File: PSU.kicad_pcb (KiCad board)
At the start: 2 copper layers, 170 x 60 mm, 55 parts, among them J1 ~12VAC_A, J10 GND, J11 -12V, J12 +5V, J2 ~12VAC_A, J3 ~12VAC_B, J4 ~12VAC_B, J9 +12V, U1 LM317_TO-220, U2 LM317_TO-220, U3 LM337_TO220

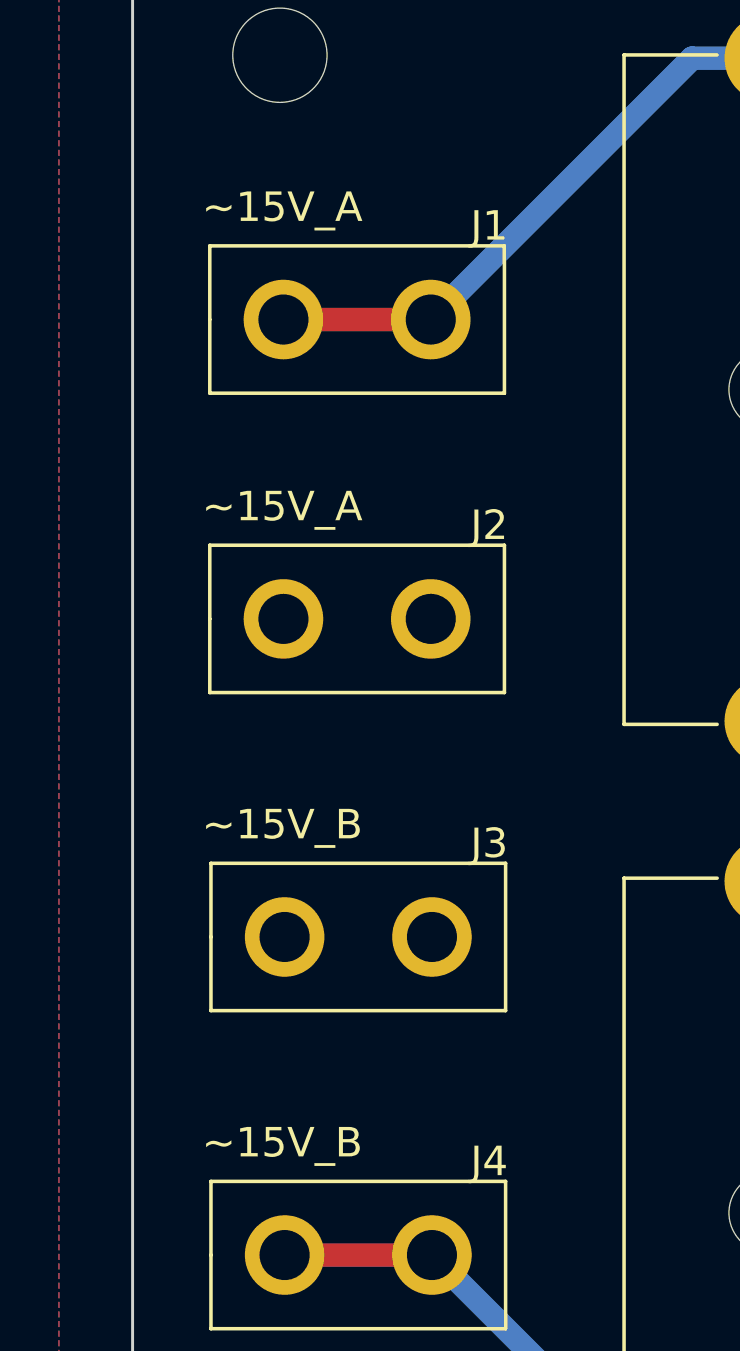
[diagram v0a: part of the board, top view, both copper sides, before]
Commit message: Swap rectifier diodes for larger ones. Change input terminal text to be more legible.
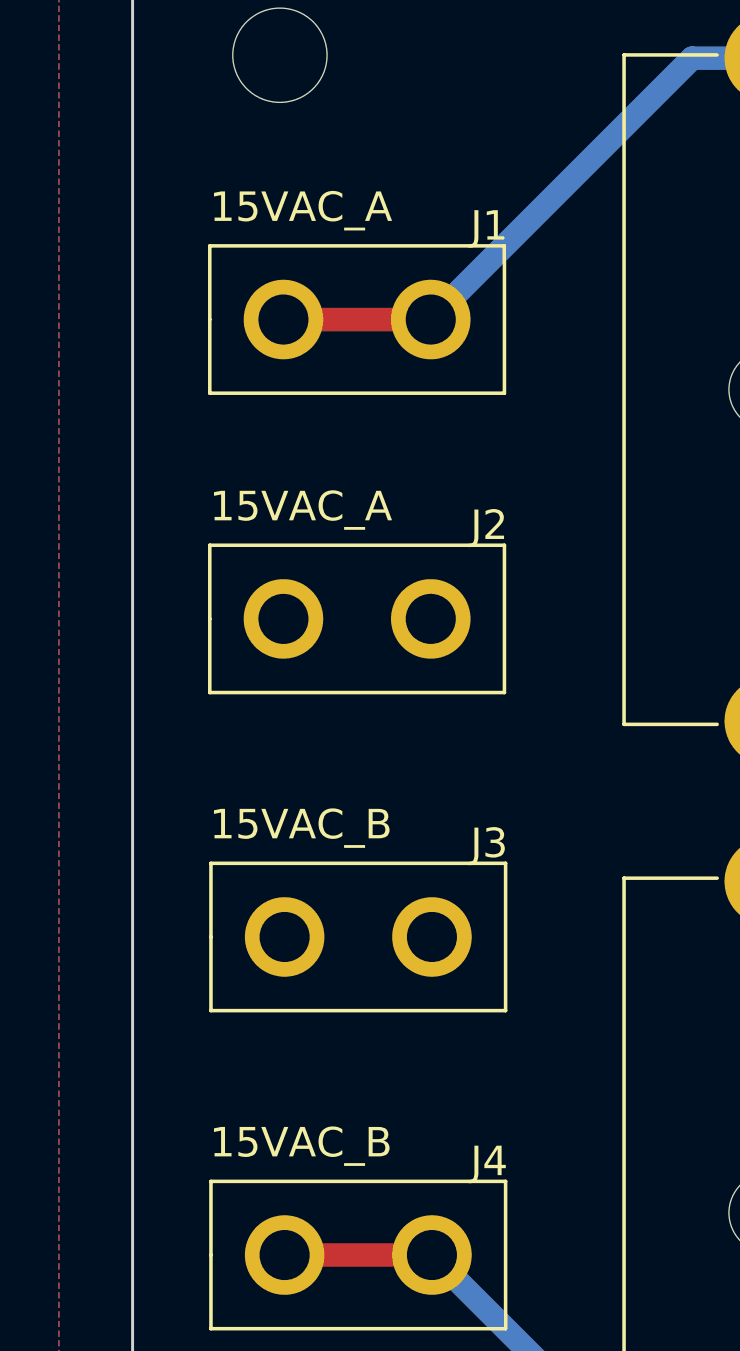
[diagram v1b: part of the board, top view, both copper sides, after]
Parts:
- D1, D2, D3, D4: value 1N4004 -> 1N5060
- F1, F2: value 6.3A fast -> fast
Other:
- board text added: "15VAC_A"
- board text added: "15VAC_B"
- board text removed: "~15V_A"
- board text removed: "~15V_B"
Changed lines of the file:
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@@
       (effects (font (size 1 1) (thickness 0.15)))
     )
-    (fp_text value "1N4004" (at 5.08 0.762) (layer "F.Fab")
+    (fp_text value "1N5060" (at 5.08 0.762) (layer "F.Fab")
       (effects (font (size 1 1) (thickness 0.15)))
     )
@@
       (effects (font (size 1 1) (thickness 0.15)))
     )
-    (fp_text value "1N4004" (at 5.08 0.762) (layer "F.Fab")
+    (fp_text value "1N5060" (at 5.08 0.762) (layer "F.Fab")
       (effects (font (size 1 1) (thickness 0.15)))
     )
@@
       (effects (font (size 1 1) (thickness 0.15)))
     )
-    (fp_text value "1N4004" (at 5.08 0.762) (layer "F.Fab")
+    (fp_text value "1N5060" (at 5.08 0.762) (layer "F.Fab")
       (effects (font (size 1 1) (thickness 0.15)))
     )
@@
       (effects (font (size 1 1) (thickness 0.15)))
     )
-    (fp_text value "6.3A fast" (at 11.25 3.81 90) (layer "F.Fab")
+    (fp_text value "fast" (at 11.25 3.81 90) (layer "F.Fab")
       (effects (font (size 1 1) (thickness 0.15)))
     )
@@
       (effects (font (size 1 1) (thickness 0.15)))
     )
-    (fp_text value "1N4004" (at 5.08 0.762) (layer "F.Fab")
+    (fp_text value "1N5060" (at 5.08 0.762) (layer "F.Fab")
       (effects (font (size 1 1) (thickness 0.15)))
     )
@@
       (effects (font (size 1 1) (thickness 0.15)))
     )
-    (fp_text value "6.3A fast" (at 12.012 -3.81 90) (layer "F.Fab")
+    (fp_text value " fast" (at 12.012 -3.81 90) (layer "F.Fab")
       (effects (font (size 1 1) (thickness 0.15)))
     )
@@
   (gr_line (start 0 0) (end 0 60) (layer "Edge.Cuts") (width 0.1))
   (gr_line (start 0 0) (end 170 0) (layer "Edge.Cuts") (width 0.1))
-  (gr_text "~15V_A" (at 5.08 10.16) (layer "F.SilkS")
+  (gr_text "15VAC_A" (at 5.715 10.16) (layer "F.SilkS")
     (effects (font (size 1 1) (thickness 0.15)))
   )
@@
     (effects (font (size 1 1) (thickness 0.15)))
   )
-  (gr_text "~15V_B" (at 5.08 31.115) (layer "F.SilkS")
+  (gr_text "15VAC_B" (at 5.715 31.115) (layer "F.SilkS")
     (effects (font (size 1 1) (thickness 0.15)))
   )
@@
     (effects (font (size 1 1) (thickness 0.15)))
   )
-  (gr_text "~15V_A" (at 5.08 20.32) (layer "F.SilkS")
+  (gr_text "15VAC_A" (at 5.715 20.32) (layer "F.SilkS")
     (effects (font (size 1 1) (thickness 0.15)))
   )
@@
     (effects (font (size 1 1) (thickness 0.15)))
   )
-  (gr_text "~15V_B" (at 5.08 41.91) (layer "F.SilkS")
+  (gr_text "15VAC_B" (at 5.715 41.91) (layer "F.SilkS")
     (effects (font (size 1 1) (thickness 0.15)))
   )

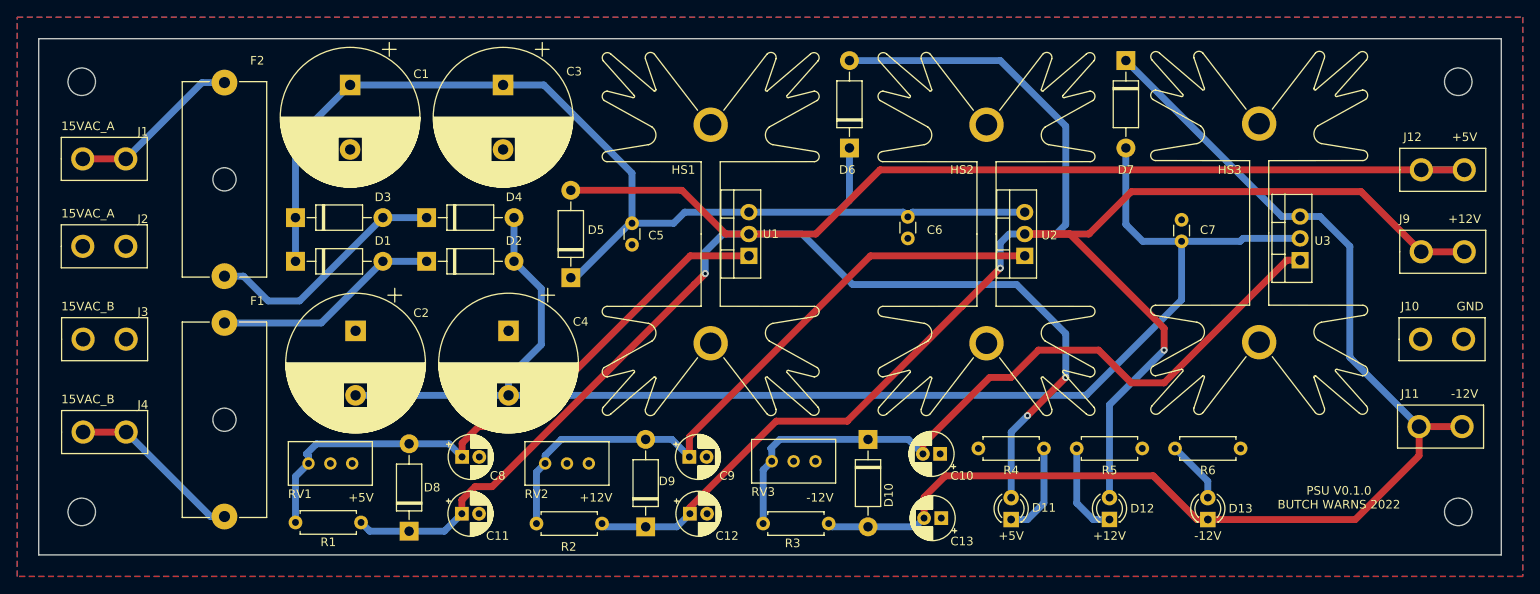
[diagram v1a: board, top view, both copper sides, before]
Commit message: Edit input label text
Change input labels for improved legibility
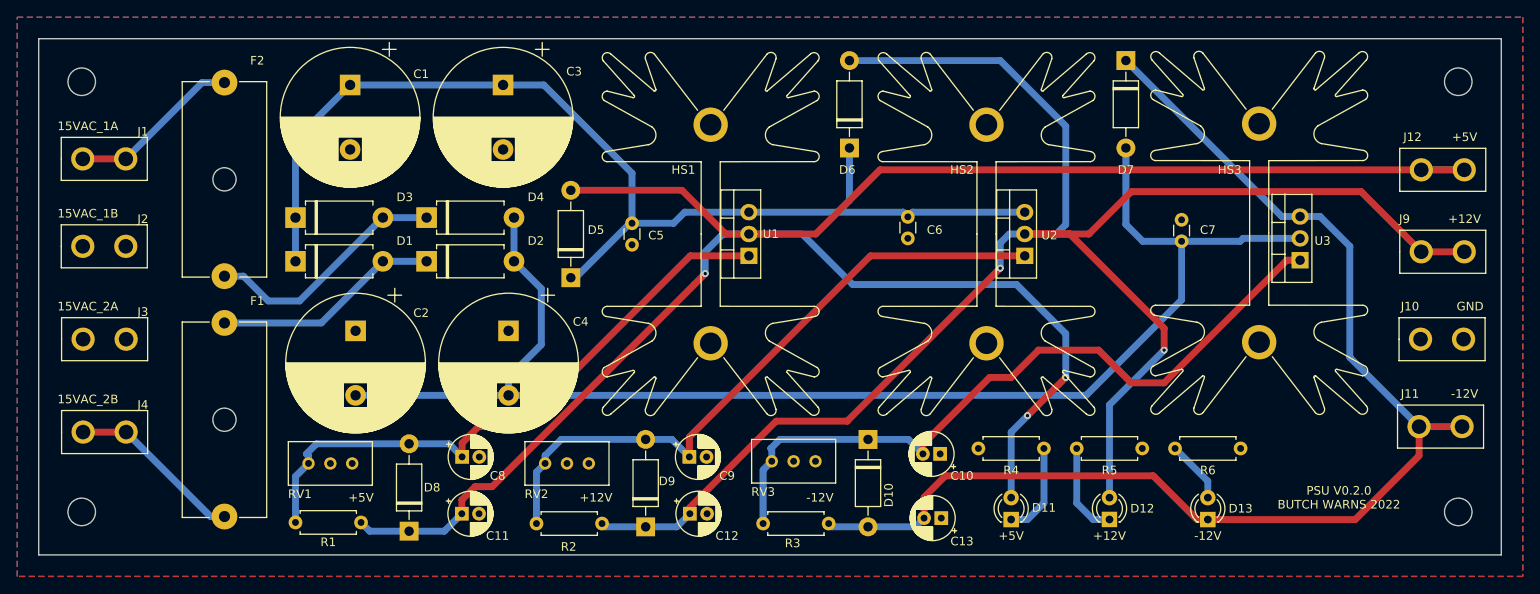
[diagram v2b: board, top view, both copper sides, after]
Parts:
- D1, D2, D3, D4: footprint Diode_THT:D_DO-41_SOD81_P10.16mm_Horizontal -> Diode_THT:D_DO-15_P10.16mm_Horizontal
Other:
- board text added: "15VAC_1A"
- board text added: "15VAC_1B"
- board text added: "15VAC_2A"
- board text added: "15VAC_2B"
- board text added: "PSU V0.2.0 BUTCH WARNS 2022"
- board text removed: "15VAC_A"
- board text removed: "15VAC_B"
- board text removed: "PSU V0.1.0 BUTCH WARNS 2022"

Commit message: Add jlcpcb order number on bottom layer
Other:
- board text added: "JLCJLCJLCJLC"
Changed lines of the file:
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@@
       (drillshape 0)
       (scaleselection 1)
-      (outputdirectory "gerber_files_PSU/")
+      (outputdirectory "gerber_files/")
     )
   )
@@
   (gr_line (start 0 0) (end 0 60) (layer "Edge.Cuts") (width 0.1))
   (gr_line (start 0 0) (end 170 0) (layer "Edge.Cuts") (width 0.1))
+  (gr_text "JLCJLCJLCJLC" (at 149.86 55.88) (layer "B.SilkS")
+    (effects (font (size 1 1) (thickness 0.15)) (justify mirror))
+  )
   (gr_text "15VAC_1A" (at 5.715 10.16) (layer "F.SilkS")
     (effects (font (size 1 1) (thickness 0.15)))
@@
     (connect_pads (clearance 0.508))
     (min_thickness 0.254) (filled_areas_thickness no)
-    (fill (thermal_gap 0.508) (thermal_bridge_width 0.508))
+    (fill yes (thermal_gap 0.508) (thermal_bridge_width 0.508))
     (polygon
       (pts
